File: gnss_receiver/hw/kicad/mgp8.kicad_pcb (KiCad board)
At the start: 8 copper layers, 100 x 75 mm, 429 parts, among them X1 FTSH-105-01-L-DV-K, X2 FTSH-105-01-L-DV-K, X3 FTSH-105-01-L-DV-K, X4 M22-2510205, X5 SM06B-GHS-TB, X6 SM04B-GHS-TB, X7 SM04B-GHS-TB, X8 SM04B-SRSS-TB

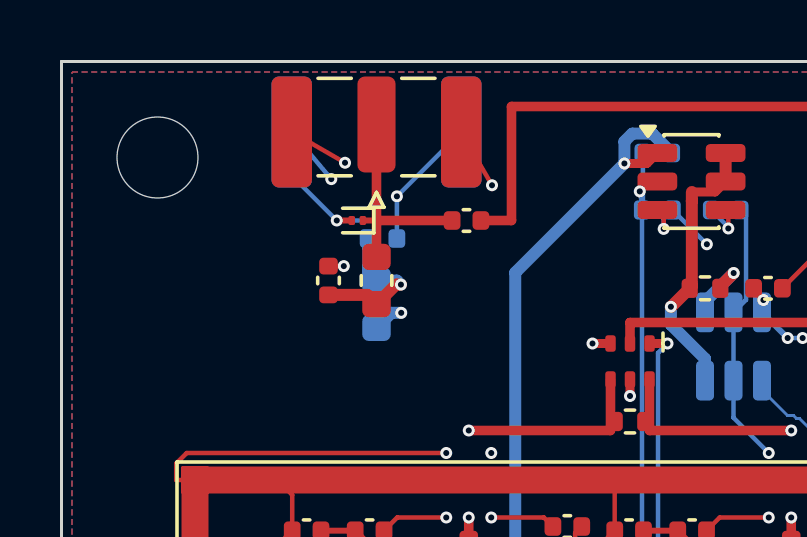
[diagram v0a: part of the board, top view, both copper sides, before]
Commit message: МГП-8: убрано наложение шелкографии у антенного разъёма — DRC без замечаний
Защитный диод VD4 сдвинут на 0,1 мм вниз вместе с отводами к антенной
линии и земле: его маркировка больше не касается метки разъёма XW1.
DRC KiCad 10 со сверкой со схемой: ни ошибок, ни предупреждений,
неразведённых 0. Масса и тепловой расчёт те же. ПЗ 4.7.4, CLAUDE.md, КД ПЗ.

Co-Authored-By: Claude Opus 5.5 <noreply@anthropic.com>
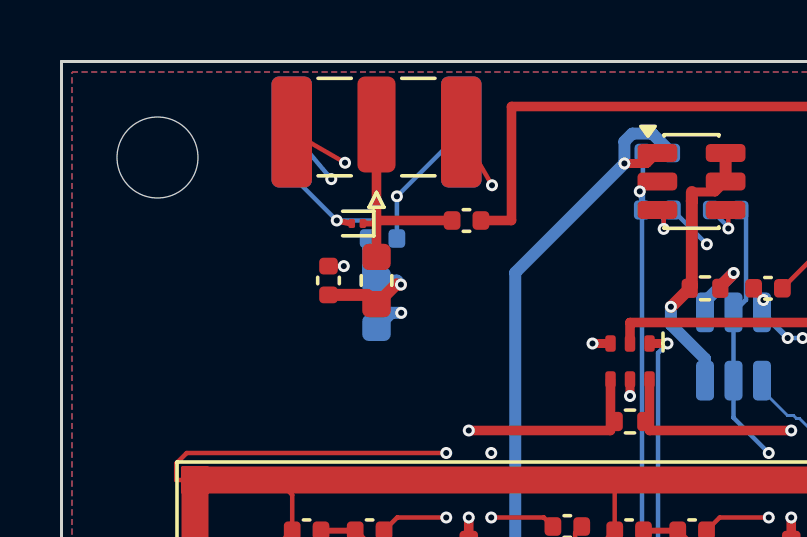
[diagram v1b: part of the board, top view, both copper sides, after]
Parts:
- moved VD4 0.10 mm to (59.9, 55.4)
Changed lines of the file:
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@@
 	(footprint "Diode_SMD:Infineon_SG-WLL-2-3_0.58x0.28_P0.36mm"
 		(layer "F.Cu")
-		(at 59.86 55.3 180)
+		(at 59.86 55.4 180)
 		(descr "Infineon  SG-WLL-2-3, 0.58x0.28x0.15mm, https://www.infineon.com/dgdl/Infineon-SG-WLL-2-3_SPO_PDF-Package-v02_00-EN.pdf?fileId=5546d46271bf4f9201723159ce71239d")
 		(tags "Infineon WLL")
@@
 	)
 	(segment
-		(start 59.635 55.3)
-		(end 59.675 55.3)
+		(start 59.635 55.4)
+		(end 59.675 55.4)
 		(width 0.15)
 		(layer "F.Cu")
@@
 	)
 	(segment
-		(start 59.635 55.3)
+		(start 59.635 55.4)
 		(end 59.175 55.3)
 		(width 0.2)
@@
 	)
 	(segment
-		(start 60.0954 55.3)
-		(end 60.0952 55.3)
+		(start 60.0954 55.4)
+		(end 60.0952 55.4)
 		(width 0.2202)
 		(layer "F.Cu")
@@
 	)
 	(segment
-		(start 60.085 55.3)
-		(end 60.5 55.3)
+		(start 60.085 55.4)
+		(end 60.5 55.4)
 		(width 0.2)
 		(locked yes)
@@
 	)
 	(segment
-		(start 60.045 55.3)
-		(end 60.0952 55.3)
+		(start 60.045 55.4)
+		(end 60.0952 55.4)
 		(width 0.192)
 		(layer "F.Cu")
